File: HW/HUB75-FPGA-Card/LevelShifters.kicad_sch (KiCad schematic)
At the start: 12 parts, among them J1 Conn_02x08_Odd_Even, J2 Conn_02x08_Odd_Even, J3 Conn_01x03, J4 Conn_01x03, J5 Conn_01x03, J6 Conn_01x03, U2 74AHCT245PW, U3 74AHCT245PW, U4 74AHCT245PW

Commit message: finish up schematic and begin routing
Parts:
- added J11, J12: Conn_01x01, Connector_Wire:SolderWire-2sqmm_1x01_D2mm_OD3.9mm, symbol Connector_Generic:Conn_01x01
- C25: renamed from C1; footprint (none) -> Capacitor_SMD:C_0603_1608Metric
- C26: renamed from C2; footprint (none) -> Capacitor_SMD:C_0603_1608Metric
- C27: renamed from C3; footprint (none) -> Capacitor_SMD:C_0603_1608Metric
- J2: renamed from J3; footprint (none) -> Connector_PinHeader_2.54mm:PinHeader_1x03_P2.54mm_Vertical
- J4, J5: footprint (none) -> Connector_PinHeader_2.54mm:PinHeader_1x03_P2.54mm_Vertical
- J7: renamed from J6; footprint (none) -> Connector_PinHeader_2.54mm:PinHeader_1x03_P2.54mm_Vertical
- renumbered J1 to J3, J2 to J6, U2 to U4, U3 to U5, U4 to U6
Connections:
- net LED1 is gone; now on net LED1_out: J2.2 (Pin_2)
- net LED2 is gone; now on net LED2_out: J4.2 (Pin_2)
- net LED3 is gone; now on net LED3_out: J5.2 (Pin_2)
- net LED4 is gone; now on net LED4_out: J7.2 (Pin_2)
- net +5V: now also J11.1 (Pin_1)
- net B1: now also U4.4 (A2); no longer J3.1 (Pin_1)
- net B2: now also U4.5 (A3); no longer J3.5 (Pin_5)
- net B3: now also U6.8 (A6); no longer J6.1 (Pin_1)
- net B4: now also U6.5 (A3); no longer J6.5 (Pin_5)
- net BLANK: now also U5.6 (A4)
- net CLKOUT: now also U5.4 (A2)
- net G1: now also U4.3 (A1); no longer J3.2 (Pin_2)
- net G2: now also U4.6 (A4); no longer J3.6 (Pin_6)
- net G3: now also U6.7 (A5); no longer J6.2 (Pin_2)
- net G4: now also U6.6 (A4); no longer J6.6 (Pin_6)
- net GND: now also U5.7 (A5), U5.8 (A6), U5.9 (A7), J12.1 (Pin_1)
- net LAT: now also U5.5 (A3)
- net R1: now also U4.2 (A0); no longer J3.3 (Pin_3)
- net R2: now also U4.7 (A5); no longer J3.7 (Pin_7)
- net R3: now also U6.9 (A7); no longer J6.3 (Pin_3)
- net R4: now also U6.4 (A2); no longer J6.7 (Pin_7)
- net ROW_CLK: now also U5.2 (A0)
- net ROW_DATA: now also U5.3 (A1)
- net STRIP1: now also U4.8 (A6)
- net STRIP2: now also U4.9 (A7)
- net STRIP3: now also U6.2 (A0)
- net STRIP4: now also U6.3 (A1)
- net RDAT_out: now reaches J3.11 (Pin_11)
- net RDAT_out: now also J6.11 (Pin_11), U5.17 (B1)
- net CLK_out: now reaches J3.13 (Pin_13)
- net CLK_out: now also J6.13 (Pin_13), U5.16 (B2)
- net LAT_out: now reaches J3.14 (Pin_14)
- net LAT_out: now also J6.14 (Pin_14), U5.15 (B3)
- net BLNK_out: now reaches J3.15 (Pin_15)
- net BLNK_out: now also J6.15 (Pin_15), U5.14 (B4)
- net RCLK_out: now reaches J3.9 (Pin_9)
- net RCLK_out: now also J6.9 (Pin_9), U5.18 (B0)
- net R3_out: now reaches U6.11 (B7)
- net R3_out: now also J6.3 (Pin_3)
- net B3_out: now reaches U6.12 (B6)
- net B3_out: now also J6.1 (Pin_1)
- net G3_out: now reaches U6.13 (B5)
- net G3_out: now also J6.2 (Pin_2)
- net G4_out: now reaches U6.14 (B4)
- net G4_out: now also J6.6 (Pin_6)
- net B4_out: now reaches U6.15 (B3)
- net B4_out: now also J6.5 (Pin_5)
- net R4_out: now reaches U6.16 (B2)
- net R4_out: now also J6.7 (Pin_7)
- net LED4_out: now reaches U6.17 (B1)
- net LED3_out: now reaches U6.18 (B0)
- net LED2_out: now reaches U4.11 (B7)
- net LED1_out: now reaches U4.12 (B6)
- net R2_out: now reaches U4.13 (B5)
- net R2_out: now also J3.7 (Pin_7)
- net G2_out: now reaches U4.14 (B4)
- net G2_out: now also J3.6 (Pin_6)
- net B2_out: now reaches U4.15 (B3)
- net B2_out: now also J3.5 (Pin_5)
- net B1_out: now reaches U4.16 (B2)
- net B1_out: now also J3.1 (Pin_1)
- net G1_out: now reaches U4.17 (B1)
- net G1_out: now also J3.2 (Pin_2)
- net R1_out: now reaches U4.18 (B0)
- net R1_out: now also J3.3 (Pin_3)
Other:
- note added: "LED1"
- note added: "LED2"
- note added: "LED3"
- note added: "LED4"
- note added: "Matrix 5V"
- note added: "Matrix GND"
- note added: "Output Connectors"
- note added: "P1"
- note added: "P2"
- note added: "Shifters"
- moved on the sheet: C25, C26, C27, J2, J3, J4, J5, J6, J7, U4, U5, U6

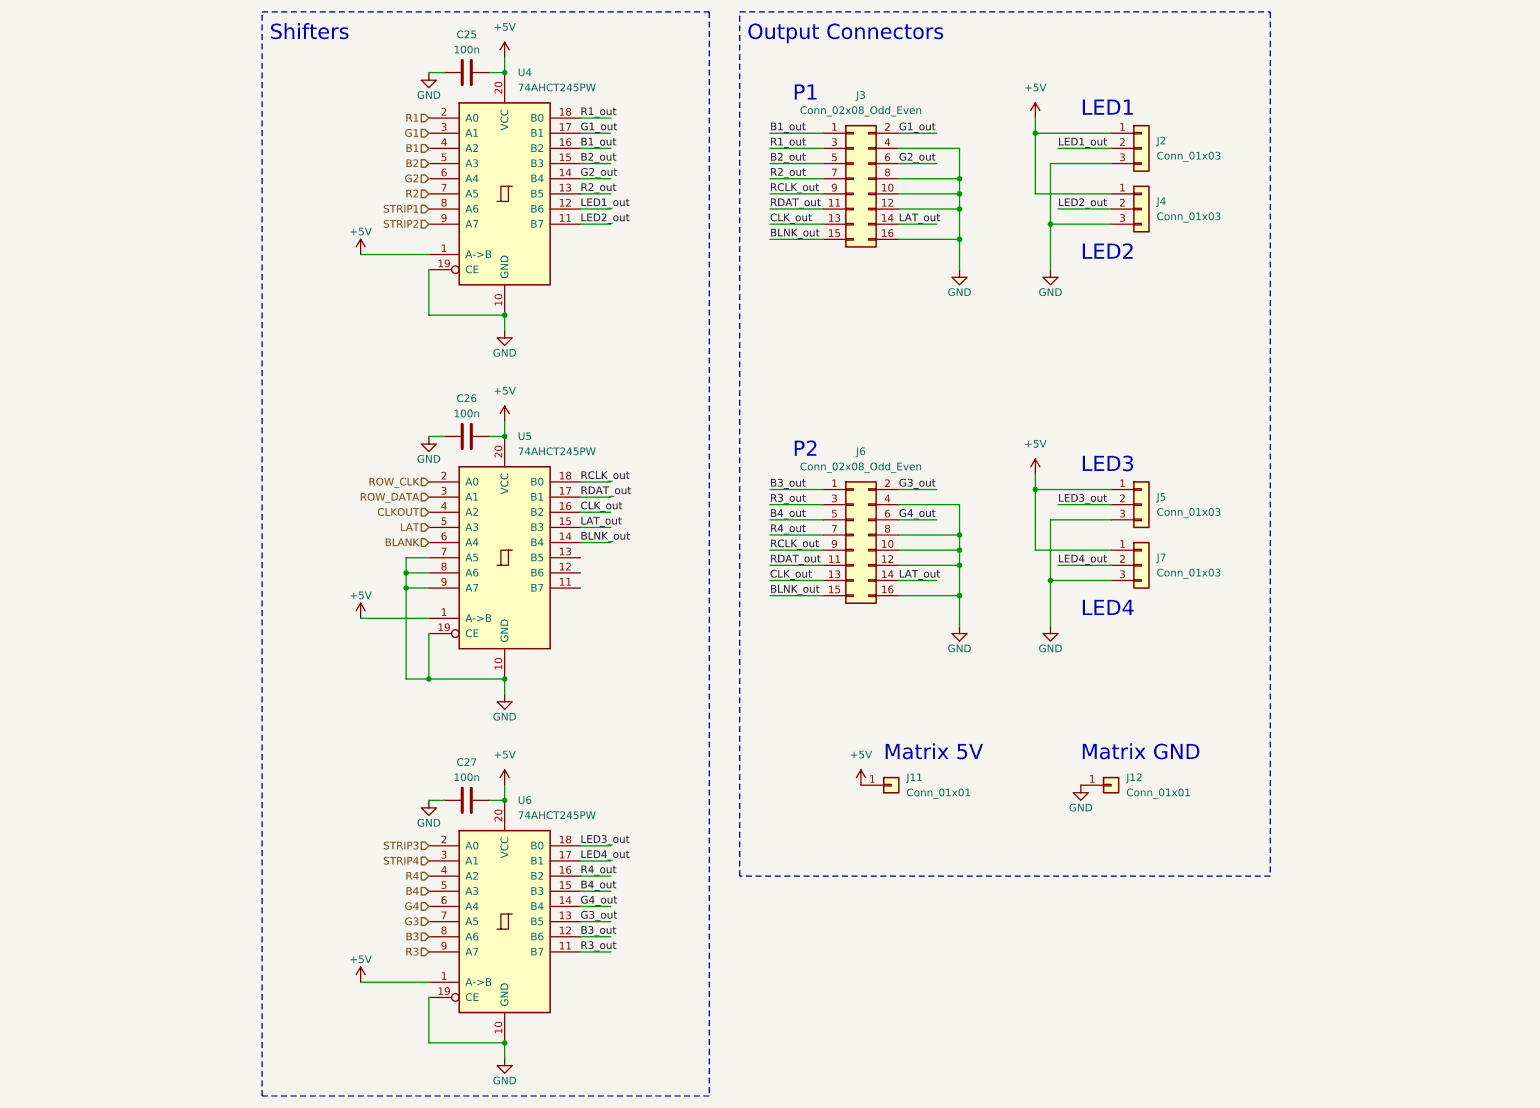
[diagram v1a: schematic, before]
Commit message: finalize pcb and generate production files for first run
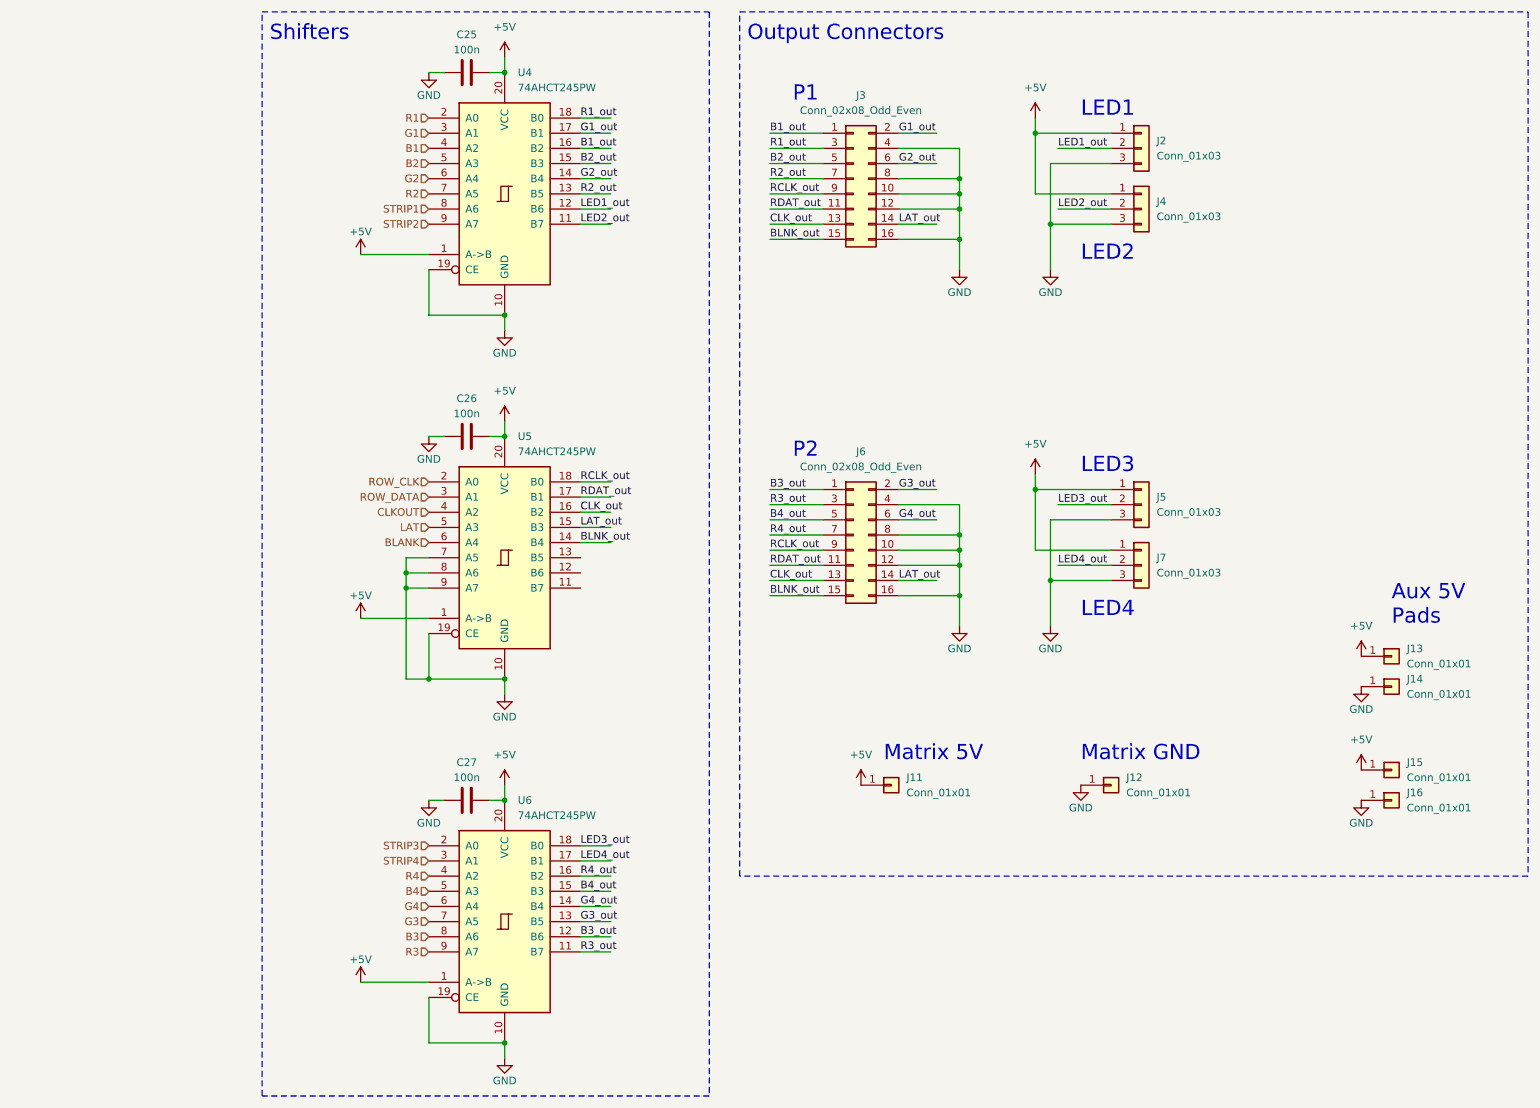
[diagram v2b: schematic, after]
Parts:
- added J13, J14, J15, J16: Conn_01x01, Connector_Wire:SolderWirePad_1x01_SMD_1x2mm, symbol Connector_Generic:Conn_01x01
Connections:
- net +5V: now also J13.1 (Pin_1), J15.1 (Pin_1)
- net GND: now also J14.1 (Pin_1), J16.1 (Pin_1)
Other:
- note added: "Aux 5V Pads"
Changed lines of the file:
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@@
     (stroke (width 0) (type default))
   )
-  (rectangle (start 146.05 13.97) (end 234.95 158.75)
+  (rectangle (start 146.05 13.97) (end 278.13 158.75)
     (stroke (width 0) (type dash))
     (fill (type none))
@@
     (effects (font (size 2.54 2.54)) (justify left bottom))
   )
+  (text "Aux 5V\nPads" (at 255.27 116.84 0)
+    (effects (font (size 2.54 2.54)) (justify left bottom))
+  )
   (text "LED4" (at 203.2 115.57 0)
     (effects (font (size 2.54 2.54)) (justify left bottom))
@@
         (path "/12c1dc17-a9d4-409d-a42e-fc131eeff0fd/eacbd1af-1c38-4bd8-912b-ae623186866b"
           (reference "#PWR048") (unit 1)
+        )
+      )
+    )
+  )
+  (symbol (lib_id "power:+5V") (at 250.19 121.92 0) (unit 1)
+    (in_bom yes) (on_board yes) (dnp no) (fields_autoplaced)
+    (property "Reference" "#PWR0102" (at 250.19 125.73 0)
+      (effects (font (size 1.27 1.27)) hide)
+    )
+    (property "Value" "+5V" (at 250.19 116.84 0)
+      (effects (font (size 1.27 1.27)))
+    )
+    (property "Footprint" "" (at 250.19 121.92 0)
+      (effects (font (size 1.27 1.27)) hide)
+    )
+    (property "Datasheet" "" (at 250.19 121.92 0)
+      (effects (font (size 1.27 1.27)) hide)
+    )
+    (pin "1")
+    (instances
+      (project "HUB75-FPGA-Card"
+        (path "/12c1dc17-a9d4-409d-a42e-fc131eeff0fd/eacbd1af-1c38-4bd8-912b-ae623186866b"
+          (reference "#PWR0102") (unit 1)
         )
       )
@@
         (path "/12c1dc17-a9d4-409d-a42e-fc131eeff0fd/eacbd1af-1c38-4bd8-912b-ae623186866b"
           (reference "J3") (unit 1)
+        )
+      )
+    )
+  )
+  (symbol (lib_id "Connector_Generic:Conn_01x01") (at 255.27 140.97 0) (unit 1)
+    (in_bom yes) (on_board yes) (dnp no) (fields_autoplaced)
+    (property "Reference" "J15" (at 257.81 139.7 0)
+      (effects (font (size 1.27 1.27)) (justify left))
+    )
+    (property "Value" "Conn_01x01" (at 257.81 142.24 0)
+      (effects (font (size 1.27 1.27)) (justify left))
+    )
+    (property "Footprint" "Connector_Wire:SolderWirePad_1x01_SMD_1x2mm" (at 255.27 140.97 0)
+      (effects (font (size 1.27 1.27)) hide)
+    )
+    (property "Datasheet" "~" (at 255.27 140.97 0)
+      (effects (font (size 1.27 1.27)) hide)
+    )
+    (pin "1")
+    (instances
+      (project "HUB75-FPGA-Card"
+        (path "/12c1dc17-a9d4-409d-a42e-fc131eeff0fd/eacbd1af-1c38-4bd8-912b-ae623186866b"
+          (reference "J15") (unit 1)
         )
       )
@@
     )
   )
+  (symbol (lib_id "power:GND") (at 250.19 127 0) (unit 1)
+    (in_bom yes) (on_board yes) (dnp no)
+    (property "Reference" "#PWR0103" (at 250.19 133.35 0)
+      (effects (font (size 1.27 1.27)) hide)
+    )
+    (property "Value" "GND" (at 250.19 130.81 0)
+      (effects (font (size 1.27 1.27)))
+    )
+    (property "Footprint" "" (at 250.19 127 0)
+      (effects (font (size 1.27 1.27)) hide)
+    )
+    (property "Datasheet" "" (at 250.19 127 0)
+      (effects (font (size 1.27 1.27)) hide)
+    )
+    (pin "1")
+    (instances
+      (project "HUB75-FPGA-Card"
+        (path "/12c1dc17-a9d4-409d-a42e-fc131eeff0fd/eacbd1af-1c38-4bd8-912b-ae623186866b"
+          (reference "#PWR0103") (unit 1)
+        )
+      )
+    )
+  )
   (symbol (lib_id "power:GND") (at 106.68 128.27 0) (unit 1)
     (in_bom yes) (on_board yes) (dnp no)
@@
     )
   )
+  (symbol (lib_id "Connector_Generic:Conn_01x01") (at 255.27 146.05 0) (unit 1)
+    (in_bom yes) (on_board yes) (dnp no) (fields_autoplaced)
+    (property "Reference" "J16" (at 257.81 144.78 0)
+      (effects (font (size 1.27 1.27)) (justify left))
+    )
+    (property "Value" "Conn_01x01" (at 257.81 147.32 0)
+      (effects (font (size 1.27 1.27)) (justify left))
+    )
+    (property "Footprint" "Connector_Wire:SolderWirePad_1x01_SMD_1x2mm" (at 255.27 146.05 0)
+      (effects (font (size 1.27 1.27)) hide)
+    )
+    (property "Datasheet" "~" (at 255.27 146.05 0)
+      (effects (font (size 1.27 1.27)) hide)
+    )
+    (pin "1")
+    (instances
+      (project "HUB75-FPGA-Card"
+        (path "/12c1dc17-a9d4-409d-a42e-fc131eeff0fd/eacbd1af-1c38-4bd8-912b-ae623186866b"
+          (reference "J16") (unit 1)
+        )
+      )
+    )
+  )
   (symbol (lib_id "power:+5V") (at 195.58 91.44 0) (unit 1)
     (in_bom yes) (on_board yes) (dnp no) (fields_autoplaced)
@@
         (path "/12c1dc17-a9d4-409d-a42e-fc131eeff0fd/eacbd1af-1c38-4bd8-912b-ae623186866b"
           (reference "J12") (unit 1)
+        )
+      )
+    )
+  )
+  (symbol (lib_id "Connector_Generic:Conn_01x01") (at 255.27 121.92 0) (unit 1)
+    (in_bom yes) (on_board yes) (dnp no) (fields_autoplaced)
+    (property "Reference" "J13" (at 257.81 120.65 0)
+      (effects (font (size 1.27 1.27)) (justify left))
+    )
+    (property "Value" "Conn_01x01" (at 257.81 123.19 0)
+      (effects (font (size 1.27 1.27)) (justify left))
+    )
+    (property "Footprint" "Connector_Wire:SolderWirePad_1x01_SMD_1x2mm" (at 255.27 121.92 0)
+      (effects (font (size 1.27 1.27)) hide)
+    )
+    (property "Datasheet" "~" (at 255.27 121.92 0)
+      (effects (font (size 1.27 1.27)) hide)
+    )
+    (pin "1")
+    (instances
+      (project "HUB75-FPGA-Card"
+        (path "/12c1dc17-a9d4-409d-a42e-fc131eeff0fd/eacbd1af-1c38-4bd8-912b-ae623186866b"
+          (reference "J13") (unit 1)
+        )
+      )
+    )
+  )
+  (symbol (lib_id "Connector_Generic:Conn_01x01") (at 255.27 127 0) (unit 1)
+    (in_bom yes) (on_board yes) (dnp no) (fields_autoplaced)
+    (property "Reference" "J14" (at 257.81 125.73 0)
+      (effects (font (size 1.27 1.27)) (justify left))
+    )
+    (property "Value" "Conn_01x01" (at 257.81 128.27 0)
+      (effects (font (size 1.27 1.27)) (justify left))
+    )
+    (property "Footprint" "Connector_Wire:SolderWirePad_1x01_SMD_1x2mm" (at 255.27 127 0)
+      (effects (font (size 1.27 1.27)) hide)
+    )
+    (property "Datasheet" "~" (at 255.27 127 0)
+      (effects (font (size 1.27 1.27)) hide)
+    )
+    (pin "1")
+    (instances
+      (project "HUB75-FPGA-Card"
+        (path "/12c1dc17-a9d4-409d-a42e-fc131eeff0fd/eacbd1af-1c38-4bd8-912b-ae623186866b"
+          (reference "J14") (unit 1)
         )
       )
@@
     )
   )
+  (symbol (lib_id "power:+5V") (at 250.19 140.97 0) (unit 1)
+    (in_bom yes) (on_board yes) (dnp no) (fields_autoplaced)
+    (property "Reference" "#PWR0104" (at 250.19 144.78 0)
+      (effects (font (size 1.27 1.27)) hide)
+    )
+    (property "Value" "+5V" (at 250.19 135.89 0)
+      (effects (font (size 1.27 1.27)))
+    )
+    (property "Footprint" "" (at 250.19 140.97 0)
+      (effects (font (size 1.27 1.27)) hide)
+    )
+    (property "Datasheet" "" (at 250.19 140.97 0)
+      (effects (font (size 1.27 1.27)) hide)
+    )
+    (pin "1")
+    (instances
+      (project "HUB75-FPGA-Card"
+        (path "/12c1dc17-a9d4-409d-a42e-fc131eeff0fd/eacbd1af-1c38-4bd8-912b-ae623186866b"
+          (reference "#PWR0104") (unit 1)
+        )
+      )
+    )
+  )
   (symbol (lib_id "power:GND") (at 182.88 57.15 0) (unit 1)
     (in_bom yes) (on_board yes) (dnp no)
@@
         )
       )
+    )
+  )
+  (symbol (lib_id "power:GND") (at 250.19 146.05 0) (unit 1)
+    (in_bom yes) (on_board yes) (dnp no)
+    (property "Reference" "#PWR0105" (at 250.19 152.4 0)
+      (effects (font (size 1.27 1.27)) hide)
+    )
+    (property "Value" "GND" (at 250.19 149.86 0)
+      (effects (font (size 1.27 1.27)))
+    )
+    (property "Footprint" "" (at 250.19 146.05 0)
+      (effects (font (size 1.27 1.27)) hide)
+    )
+    (property "Datasheet" "" (at 250.19 146.05 0)
+      (effects (font (size 1.27 1.27)) hide)
+    )
+    (pin "1")
+    (instances
+      (project "HUB75-FPGA-Card"
+        (path "/12c1dc17-a9d4-409d-a42e-fc131eeff0fd/eacbd1af-1c38-4bd8-912b-ae623186866b"
+          (reference "#PWR0105") (unit 1)
+        )
+      )
